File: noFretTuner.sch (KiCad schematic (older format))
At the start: 4 parts, among them J1 Conn_01x02, J2 DC Supply Connection, J3 Battery Connection, U1 STM32F091RCT6

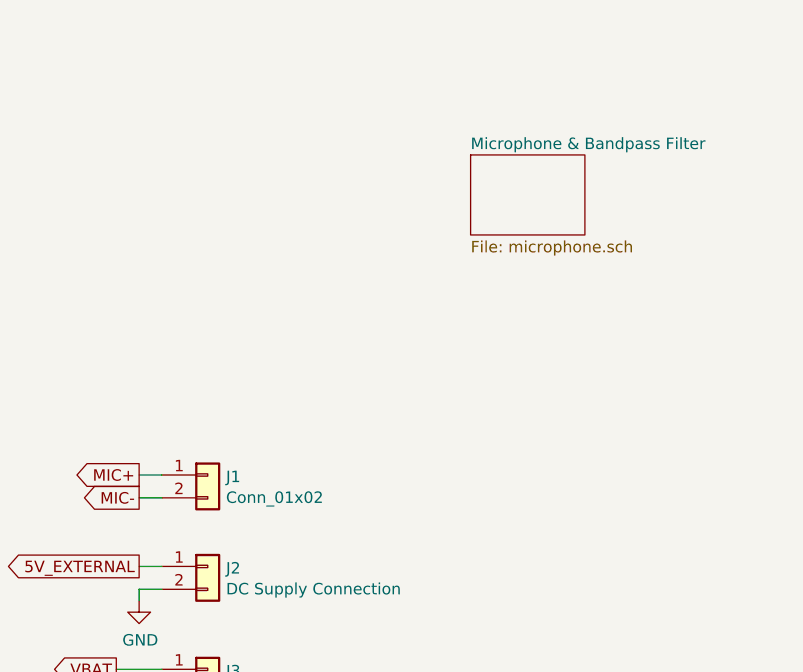
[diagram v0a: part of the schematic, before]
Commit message: Slight Placement Changes
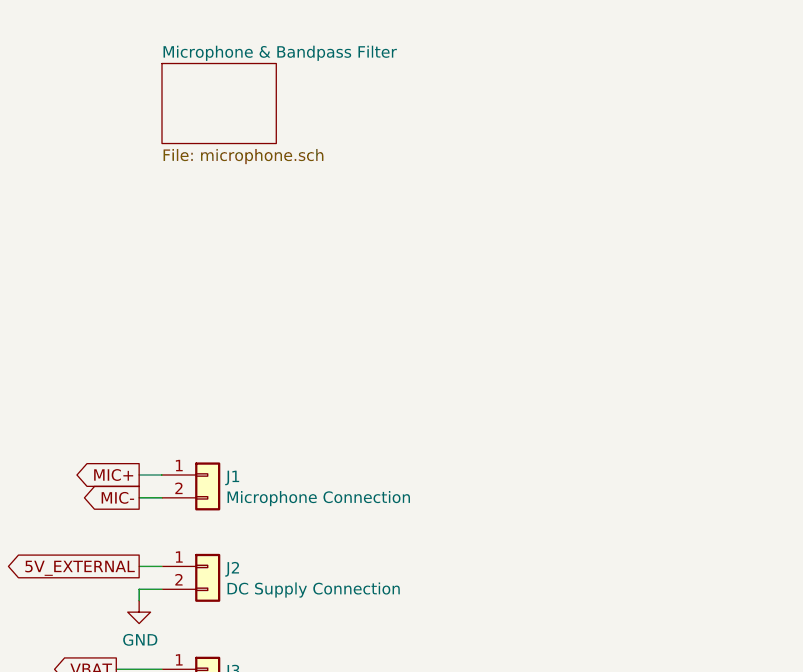
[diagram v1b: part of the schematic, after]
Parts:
- J1: value Conn_01x02 -> Microphone Connection
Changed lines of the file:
@@
 $EndComp
 $Sheet
-S 9050 1100 500  350
+S 7700 700  500  350
 U 6207A6E4
 F0 "Microphone & Bandpass Filter" 50
@@
 P 7900 2500
 F 0 "J1" H 7980 2492 50  0000 L CNN
-F 1 "Conn_01x02" H 7980 2401 50  0000 L CNN
+F 1 "Microphone Connection" H 7980 2401 50  0000 L CNN
 F 2 "TerminalBlock_TE-Connectivity:TerminalBlock_TE_282834-2_1x02_P2.54mm_Horizontal" H 7900 2500 50  0001 C CNN
 F 3 "~" H 7900 2500 50  0001 C CNN

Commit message: Motor Controller Done
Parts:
- added J?: Stepper Motor Connection, symbol Connector_Generic:Conn_01x04
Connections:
- new net A1: J?.1 (Pin_1)
- new net A2: J?.2 (Pin_2)
- new net B1: J?.3 (Pin_3)
- new net B2: J?.4 (Pin_4)
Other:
- moved on the sheet: U1A
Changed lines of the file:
@@
-$Comp
-L STM32F091RCT6:STM32F091RCT6 U1
-U 1 1 62040D0D
-P 750 1100
-F 0 "U1" H 2250 1487 60  0000 C CNN
-F 1 "STM32F091RCT6" H 2250 1381 60  0000 C CNN
-F 2 "LQFP64-10x10mm" H 1650 1340 60  0001 C CNN
-F 3 "" H 750 1100 60  0000 C CNN
-	1    750  1100
-	1    0    0    -1
-$EndComp
 $Comp
 L STM32F091RCT6:STM32F091RCT6 U1
@@
 F 3 "" H 4150 950 60  0000 C CNN
 	2    4150 950
-	1    0    0    -1
-$EndComp
-$Sheet
-S 7700 700  500  350
-U 6207A6E4
-F0 "Microphone & Bandpass Filter" 50
-F1 "microphone.sch" 50
-$EndSheet
-$Comp
-L Connector_Generic:Conn_01x02 J1
-U 1 1 620A7E14
-P 7900 2500
-F 0 "J1" H 7980 2492 50  0000 L CNN
-F 1 "Microphone Connection" H 7980 2401 50  0000 L CNN
-F 2 "TerminalBlock_TE-Connectivity:TerminalBlock_TE_282834-2_1x02_P2.54mm_Horizontal" H 7900 2500 50  0001 C CNN
-F 3 "~" H 7900 2500 50  0001 C CNN
-	1    7900 2500
 	1    0    0    -1
 $EndComp
@@
 Wire Wire Line
 	7600 3000 7600 3050
+$Comp
+L Connector_Generic:Conn_01x02 J1
+U 1 1 620A7E14
+P 7900 2500
+F 0 "J1" H 7980 2492 50  0000 L CNN
+F 1 "Microphone Connection" H 7980 2401 50  0000 L CNN
+F 2 "TerminalBlock_TE-Connectivity:TerminalBlock_TE_282834-2_1x02_P2.54mm_Horizontal" H 7900 2500 50  0001 C CNN
+F 3 "~" H 7900 2500 50  0001 C CNN
+	1    7900 2500
+	1    0    0    -1
+$EndComp
+$Sheet
+S 7700 700  500  350
+U 6207A6E4
+F0 "Microphone & Bandpass Filter" 50
+F1 "microphone.sch" 50
+$EndSheet
+$Comp
+L STM32F091RCT6:STM32F091RCT6 U1
+U 1 1 62040D0D
+P 800 950
+F 0 "U1" H 2300 1337 60  0000 C CNN
+F 1 "STM32F091RCT6" H 2300 1231 60  0000 C CNN
+F 2 "LQFP64-10x10mm" H 1700 1190 60  0001 C CNN
+F 3 "" H 800 950 60  0000 C CNN
+	1    800  950
+	1    0    0    -1
+$EndComp
+$Comp
+L Connector_Generic:Conn_01x04 J?
+U 1 1 623ABF0F
+P 7900 4000
+F 0 "J?" H 7980 3992 50  0000 L CNN
+F 1 "Stepper Motor Connection" H 7980 3901 50  0000 L CNN
+F 2 "" H 7900 4000 50  0001 C CNN
+F 3 "~" H 7900 4000 50  0001 C CNN
+	1    7900 4000
+	1    0    0    -1
+$EndComp
+Text GLabel 7500 3900 0    50   Input ~ 0
+A1
+Text GLabel 7500 4000 0    50   Input ~ 0
+A2
+Text GLabel 7500 4100 0    50   Input ~ 0
+B1
+Text GLabel 7500 4200 0    50   Input ~ 0
+B2
+Wire Wire Line
+	7500 3900 7700 3900
+Wire Wire Line
+	7500 4000 7700 4000
+Wire Wire Line
+	7500 4100 7700 4100
+Wire Wire Line
+	7500 4200 7700 4200
 $EndSCHEMATC

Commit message: First Draft Complete
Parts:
- removed U1: STM32F091RCT6, LQFP64-10x10mm, symbol STM32F091RCT6:STM32F091RCT6
- added C? (x2): C_Small, symbol Device:C_Small
- added C? (x8): 0.1 uF, symbol Device:C_Small
- added C?: 100 uF, symbol Device:CP1_Small
- added C?: 10 nF, symbol Device:C_Small
- added C?: 0.47 uF, symbol Device:C_Small
- added FB?: Ferrite_Bead_Small, symbol Device:Ferrite_Bead_Small
- added J?: Programmer Header, symbol Connector_Generic:Conn_02x05_Odd_Even
- added J?: LCD Connection, symbol Connector_Generic:Conn_01x09
- added R? (x8): 10 k, symbol Device:R_Small_US
- added R? (x2): 4.7 k, symbol Device:R_Small_US
- added R?: 100k, symbol Device:R_Small_US
- added R?: 1 M, Resistor_SMD:R_0805_2012Metric_Pad1.15x1.40mm_HandSolder, symbol Device:R_Small_US
- added R? (x2): 100 m, Resistor_SMD:R_0805_2012Metric_Pad1.15x1.40mm_HandSolder, symbol Device:R_Small_US
- added R? (x5): 10 k, Resistor_SMD:R_0805_2012Metric_Pad1.15x1.40mm_HandSolder, symbol Device:R_Small_US
- added R?: 1.5 k, Resistor_SMD:R_0805_2012Metric_Pad1.15x1.40mm_HandSolder, symbol Device:R_Small_US
- added RV?: 10k, symbol Device:R_POT_US
- added SW? (x5): Switch_SW_Push, symbol STM32F091RCTx:Switch_SW_Push
- added U1: STM32F091RCTx, Package_QFP:LQFP-64_10x10mm_P0.5mm, symbol STM32F091RCTx:STM32F091RCTx
- added U?: DRV8825PWP, Texas_Instruments-DRV8825PWP-*, symbol DRV8825PWP:DRV8825PWP
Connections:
- net GND: now also C?.2, C?.2, C?.2, C?.2, C?.2, C?.2, C?.2, C?.2, C?.2, C?.2, C?.2, J?.2 (Pin_2), J?.3 (Pin_3), J?.4 (Pin_4), R?.1, R?.1, R?.2, R?.2, R?.2, R?.2, RV?.3, SW?.1, U1.12 (VSSA), U1.18 (VSS), U1.31 (VSS), U1.47 (VSS), U1.63 (VSS), U?.14 (GND), U?.28 (GND), U?.29 (GND)
- net A1 renamed motor_A1
- net motor_A1: now also U?.5 (AOUT1)
- net A2 renamed motor_A2
- net motor_A2: now also U?.7 (AOUT2)
- net B1 renamed motor_B1
- net motor_B1: now also U?.10 (BOUT1)
- net B2 renamed motor_B2
- net motor_B2: now also U?.8 (BOUT2)
- new net: R?.1, R?.2, SW?.1 (x4)
- new net: C?.1, R?.1, U?.3 (VCP)
- new net: C?.1, U?.1 (CP1)
- new net: C?.2, U?.2 (CP2)
- new net: R?.2, U?.6 (ISENA)
- new net: C?.1, RV?.1, U?.15 (V3P3OUT)
- new net: RV?.2, U?.12 (AVREF), U?.13 (BVREF)
- new net: R?.2, U?.18 (NFAULT)
- new net: R?.2, U?.9 (ISENB)
- new net +3V3: C?.1, FB?.2, J?.1 (Pin_1), J?.8 (Pin_8), R?.1, R?.1, R?.1, R?.1, R?.1, R?.1, R?.1, SW?.2, SW?.2, SW?.2, SW?.2, U1.1 (VBAT), U1.19 (VDD), U1.32 (VDD), U1.48 (VDDIO2), U1.64 (VDD)
- new net 3v3a: C?.1, FB?.1, U1.13 (VDDA)
- new net 9V: C?.1, C?.1, C?.1, C?.2, R?.2, U?.11 (VMB), U?.4 (VMA)
- new net ADC: U1.26 (PB0)
- new net Boost_EN: U1.39 (PC8)
- new net Button1: C?.1, R?.1, U1.28 (PB2)
- new net Button2: C?.1, R?.1, U1.55 (PB3)
- new net Button3: C?.1, R?.1, U1.56 (PB4)
- new net Button4: C?.1, R?.1, U1.57 (PB5)
- new net I2C_SCA: R?.2, U1.30 (PB11)
- new net I2C_SCL: R?.2, U1.29 (PB10)
- new net LCD_DC: J?.5 (Pin_5), U1.17 (PA3)
- new net LCD_RESET: J?.4 (Pin_4), U1.16 (PA2)
- new net SPI_MOSI: J?.6 (Pin_6), U1.23 (PA7)
- new net SPI_NSS: J?.3 (Pin_3), U1.20 (PA4)
- new net SPI_SCK: J?.7 (Pin_7), U1.21 (PA5)
- new net SWCLK_IN: J?.6 (Pin_6)
- new net SWDIO_IN: J?.2 (Pin_2)
- new net motor_DECAY: U1.24 (PC4), U?.19 (DECAY)
- new net motor_DIR: U1.11 (PC3), U?.20 (DIR)
- new net motor_MODE0: U?.24 (MODE0)
- new net motor_MODE1: U?.25 (MODE1)
- new net motor_MODE2: U1.25 (PC5), U?.26 (MODE2)
- new net motor_STEP: U1.41 (PA8), U?.22 (STEP)
- new net motor_nENBL: R?.2, U1.8 (PC0), U?.21 (NENBL)
- new net motor_nFAULT: R?.1, R?.2, U1.38 (PC7)
- new net motor_nHOME: R?.2, U1.37 (PC6), U?.27 (NHOME)
- new net motor_nRESET: R?.2, U1.9 (PC1), U?.16 (NRESET)
- new net motor_nSLEEP: R?.1, R?.2, U1.10 (PC2), U?.17 (NSLEEP)
- new net nRST: C?.1, J?.1 (Pin_1), R?.2, SW?.2, U1.7 (NRST)
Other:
- note added: "Analog Supply"
- note added: "Buttons"
- note added: "Input Headers"
- note added: "Main Microcontroller"
- note added: "Motor Driver"
- note added: "Output Headers"
- note added: "nRESET Button"
- moved on the sheet: J1, J2, J3, J?

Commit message: Oscillator and Decouple Caps
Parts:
- added C? (x4): 0.1 uF, symbol Device:C_Small
- added C?: 4.7 uF, symbol Device:C_Small
- added C?: 0.01 uF, symbol Device:C_Small
- added C? (x2): 12 pF, symbol Device:C_Small
- added C? (x2): 20 pF, symbol Device:C_Small
- added R?: 100 k, symbol Device:R_Small_US
- added R?: 380, symbol Device:R_Small_US
- added Y?: 32.768 khz (12.5pF), symbol Device:Crystal
- added Y?: 8 Mhz (20pF), symbol Device:Crystal
- C?: value C_Small -> 1 uF
- C?: value C_Small -> 4.7 uF
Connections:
- net +3V3: now also C?.1, C?.1, C?.1, C?.1, C?.1
- net 3v3a: now also C?.1
- net GND: now also C?.2, C?.2, C?.2, C?.2, C?.2, C?.2, C?.2, C?.2, C?.2, C?.2, R?.2
- net OSC32_IN: now reaches U1.49 (PA14)
- net OSC32_IN: now also C?.1, Y?.1
- net OSC_IN: now reaches U1.5 (PF0)
- net OSC_IN: now also C?.1, Y?.1
- net OSC32_OUT: now reaches U1.50 (PA15)
- net OSC32_OUT: now also C?.1, Y?.2
- net OSC_OUT: now reaches U1.6 (PF1)
- net OSC_OUT: now also R?.1
- net at U1.60 (PF11): now also R?.1
- new net: C?.1, R?.2, Y?.2
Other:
- note added: "Boot Pin"
- note added: "Decoubling Caps & Analog Supply"
- note added: "Oscillator Circuits"
- note removed: "Analog Supply"
- moved on the sheet: C?, FB?, R?, U1

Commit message: Ready for PCB Layout
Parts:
- added J1: Conn_01x05, symbol Connector_Generic:Conn_01x05
- added J2: Conn_01x03, symbol Connector_Generic:Conn_01x03
- SW1: renamed from SW?; footprint (none) -> Button_Switch_SMD:SW_Push_1P1T_NO_6x6mm_H9.5mm
- gave numbers to parts that had none: 57
- renumbered J1 to J4, J2 to J5, J3 to J6
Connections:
- net +3V3: now also J1.1 (Pin_1), J2.1 (Pin_1)
- net GND: now also J1.5 (Pin_5), J2.3 (Pin_3)
- net ext_Button1: now reaches U1.58 (PB6)
- net ext_Button1: now also J1.2 (Pin_2)
- net ext_Button2: now reaches U1.59 (PB7)
- net ext_Button2: now also J1.3 (Pin_3)
- net ext_Button3: now reaches U1.61 (PB8)
- net ext_Button3: now also J1.4 (Pin_4)
- net ext_Button4: now reaches U1.62 (PB9)
- net ext_Button4: now also J2.2 (Pin_2)
- net 3v3a renamed +3.3VA
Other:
- moved on the sheet: R11, R9
